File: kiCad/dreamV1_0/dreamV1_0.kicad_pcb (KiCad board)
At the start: 2 copper layers, 80 x 80 mm, 37 parts, among them IC1 TGS2611-C00, J1 GPIO, J11 10132328-10011LF, J2 Qwiic_Vertical, J3 679305124022, J4 Qwiic_Vertical, J5 M20-7830542, J6 Qwiic_Vertical, J7 5013310607, J8 Qwiic_Vertical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

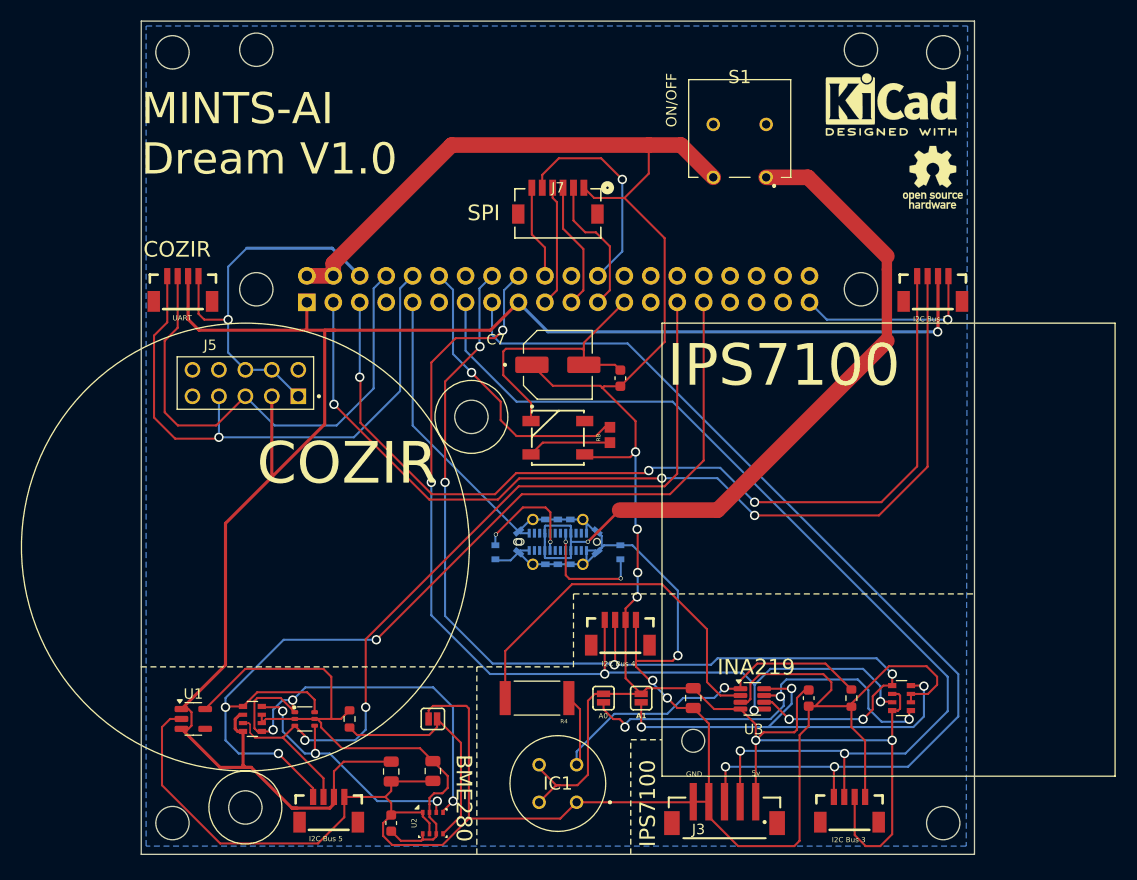
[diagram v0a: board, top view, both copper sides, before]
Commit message: Add files via upload
Type C moved to be above the GPIO, new switch, subtle mounting hole, and border changes.
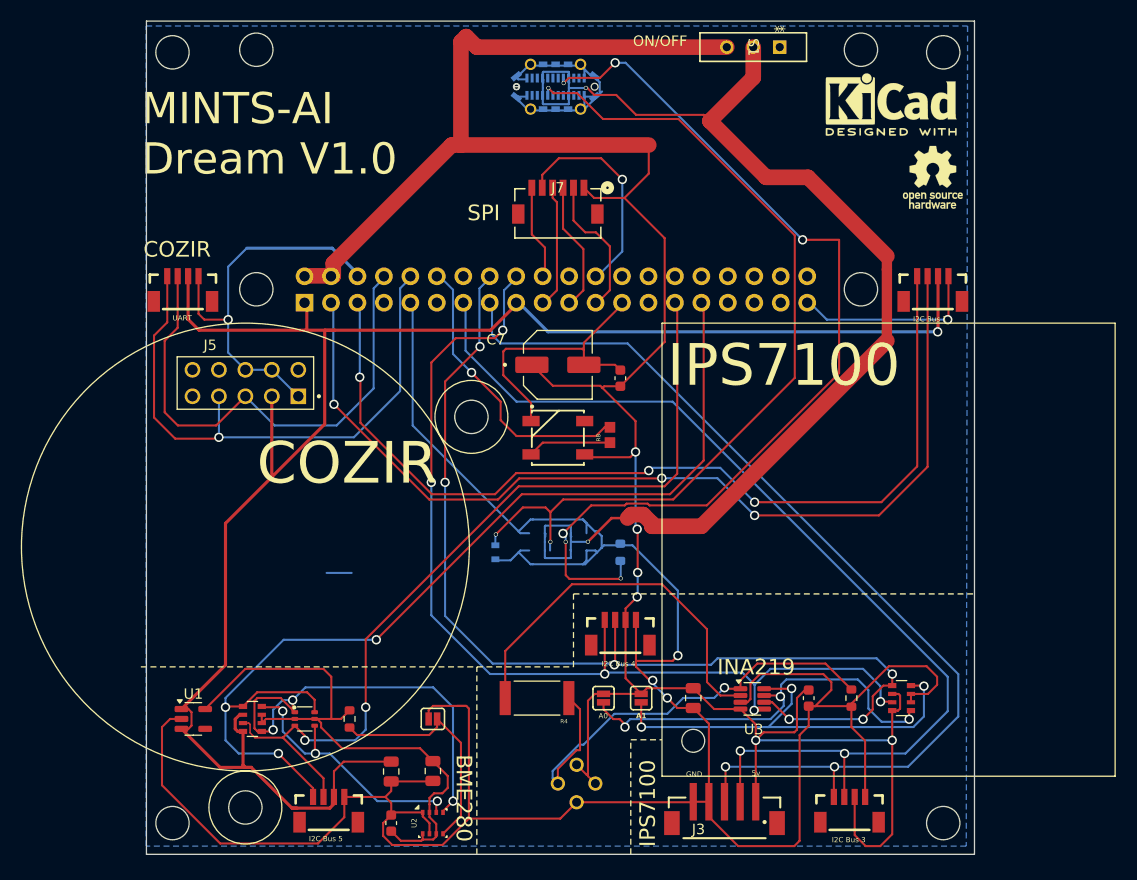
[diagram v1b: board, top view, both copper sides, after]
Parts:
- IC1: footprint KiCad:TGS2611C00 -> footprints1:TGS2611-C00_FGS; moved to B.Cu
- R7: footprint downloaded:RC0603N_YAG-L -> Resistor_SMD:R_0603_1608Metric
- S1: value AB11AH-FC -> NKK236; footprint downloaded:AB11AHFC -> footprints2:SWITCH_NK236_APM
- moved J11 43.7 mm to (89.8, 56.3)
- moved S1 12.6 mm to (111.3, 52.5), turned to -90 degrees
- moved J1 0.22 mm to (65.7, 77.0)
- turned IC1 to 180 degrees
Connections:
- S1 pad 2: unconnected-(S1-Pad2) -> +5V
- S1 pad 3: +5V -> unconnected-(S1-B-Pad3)
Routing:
- net Net-(J11-CC1): track 11.2 -> 92.1 mm, vias 2 -> 6
- net Net-(J11-CC2): track 11.1 -> 84.0 mm, vias 2 -> 3
- net /5V_BUS_USB: track 73.1 -> 117.4 mm, vias 1 -> 2
- net GND: track 355.2 -> 383.6 mm
- net +5V: track 210.8 -> 233.3 mm
- net /INA+: track 39.7 -> 46.1 mm
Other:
- board size 80 x 80 mm -> 79.5 x 80 mm

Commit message: reverted file structure to contain both v1 and v2
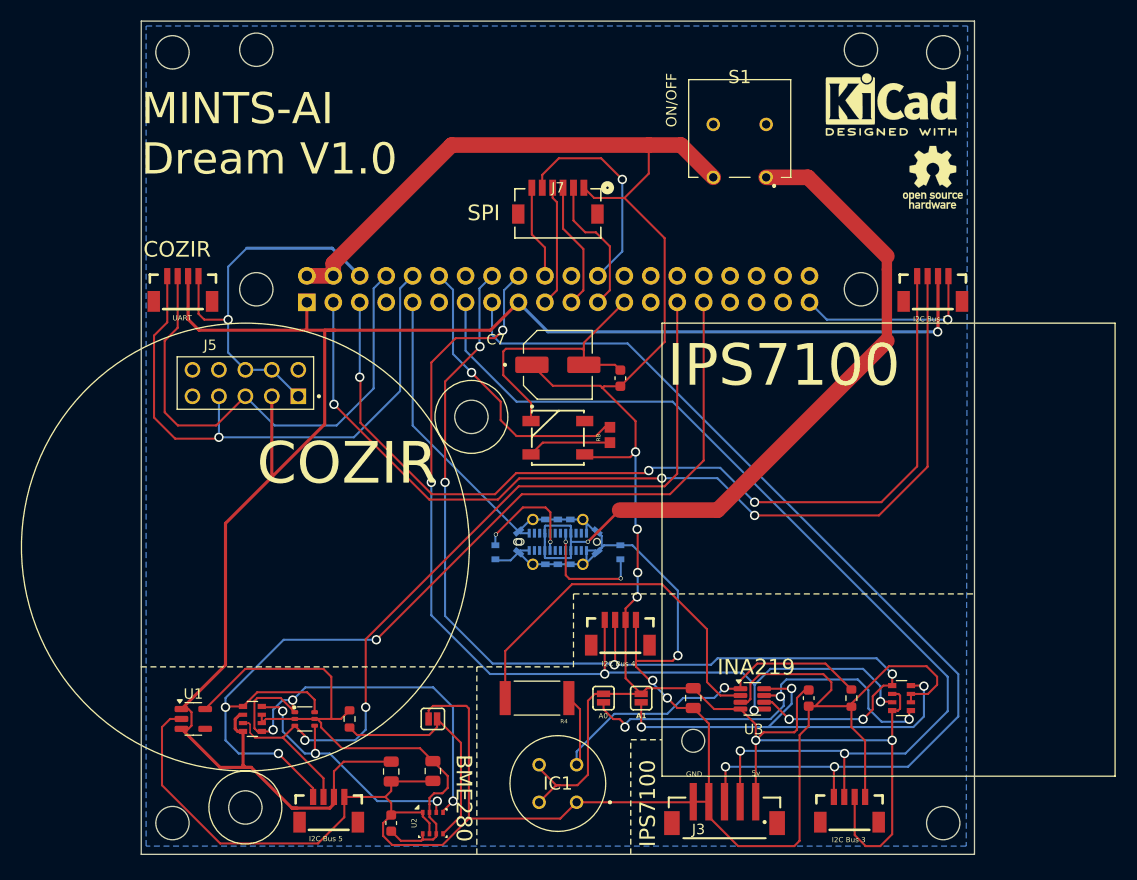
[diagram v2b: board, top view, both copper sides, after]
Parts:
- IC1: footprint footprints1:TGS2611-C00_FGS -> KiCad:TGS2611C00; moved to F.Cu
- R7: footprint Resistor_SMD:R_0603_1608Metric -> downloaded:RC0603N_YAG-L
- S1: value NKK236 -> AB11AH-FC; footprint footprints2:SWITCH_NK236_APM -> downloaded:AB11AHFC
- moved J11 43.7 mm to (90.0, 100.0)
- moved S1 12.6 mm to (110.0, 65.0), turned to 180 degrees
- moved J1 0.22 mm to (65.9, 77.0)
- turned IC1 to 0 degrees
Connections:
- S1 pad 2: +5V -> unconnected-(S1-Pad2)
- S1 pad 3: unconnected-(S1-B-Pad3) -> +5V
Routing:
- net Net-(J11-CC1): track 92.1 -> 11.2 mm, vias 6 -> 2
- net Net-(J11-CC2): track 84.0 -> 11.1 mm, vias 3 -> 2
- net /5V_BUS_USB: track 117.4 -> 73.1 mm, vias 2 -> 1
- net GND: track 383.6 -> 355.2 mm
- net +5V: track 233.3 -> 210.8 mm
- net /INA+: track 46.1 -> 39.7 mm
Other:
- board size 79.5 x 80 mm -> 80 x 80 mm
